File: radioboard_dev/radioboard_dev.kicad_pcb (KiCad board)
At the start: 2 copper layers, 92 parts, among them J1 Conn_01x02, J2 Conn_01x02, J3 Conn_01x04, J4 Conn_01x04, J5 Conn_01x04, J6 Conn_01x04, U10 STM32WL55CCUx, U2 TPS73733QDRBRQ1, U5 MCP73831T-2ACI_OT, U7 MAX17048G_T10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

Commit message: footprints
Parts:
- removed R36: ~, parts:R0402
- added U1: ACS722LLCTR-05AB-T, parts:SOIC127P600X175-8N, F.Cu at (86.2, 83.2)
- moved CN12 49.9 mm to (53.3, 26.1), turned to 180 degrees
- moved C10 42.1 mm to (99.1, 55.4), turned to 180 degrees
- moved C18 32.6 mm to (103.8, 47.9), turned to 90 degrees
- moved U10 29.9 mm to (104.5, 53.1)
- moved C28 29.4 mm to (105.2, 47.9), turned to -90 degrees
- moved C23 28.8 mm to (107.2, 47.9), turned to 90 degrees
- moved C26 18.1 mm to (105.3, 45.6), turned to -90 degrees
- moved J4 17.7 mm to (25.3, 38.9)
- moved J3 17.0 mm to (25.8, 64.5)
- moved LED4 16.6 mm to (87.0, 58.3), turned to 90 degrees
- moved J6 8.59 mm to (25.9, 24.4)
- moved R26 5.48 mm to (96.7, 73.8)
- moved LED2 5.20 mm to (91.0, 58.4), turned to 90 degrees
- moved LED3 4.99 mm to (92.4, 58.5), turned to 90 degrees
- moved J5 4.89 mm to (24.4, 52.8)
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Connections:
- net /U_STM32_microcontroller_IOs/BUT1 renamed BUT1
- C10 pad 1: Net-(U10-VBAT) -> +3.3V
- C18 pad 1: Net-(U10-VBAT) -> +3.3V
- C23 pad 1: Net-(U10-VBAT) -> +3.3V
- J5 pad 1: unconnected-(J5-Pin_1-Pad1) -> SPI1_MOSI
- J5 pad 2: unconnected-(J5-Pin_2-Pad2) -> SPI1_MISO
- J5 pad 4: unconnected-(J5-Pin_4-Pad4) -> SPI1_NSS
- R34 pad 1: /U_STM32_microcontroller_IOs/LED3 -> LED2
- R35 pad 1: /U_STM32_microcontroller_IOs/LED2 -> LED1
- U10 pad 11: Net-(U10-VBAT) -> +3.3V
- U10 pad 12: /U_STM32_microcontroller_IOs/LED1 -> LED1
- U10 pad 13: /U_STM32_microcontroller_IOs/LED2 -> LED2
- U10 pad 14: /U_STM32_microcontroller_IOs/LED3 -> unconnected-(U10-PA6-Pad14)
- U10 pad 37: Net-(U10-VBAT) -> +3.3V
- U10 pad 44: Net-(U10-VBAT) -> +3.3V
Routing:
- net +3.3V: track 0.00 -> 4.14 mm
- net Net-(U10-VDDA): track 0.00 -> 3.96 mm

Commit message: all footprints done
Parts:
- removed U7: MAX17048G_T10, parts:SON50P200X200X80-9N
- removed U9: TPS22917DBVR, parts:SOT95P280X145-6N
- added J9: Conn_01x04, Connector_PinHeader_2.54mm:PinHeader_1x04_P2.54mm_Vertical, F.Cu at (23.7, 69.0)
- added L1: ~, Inductor_SMD:L_0603_1608Metric, F.Cu at (92.6, 43.3)
- added L12: ~, Inductor_SMD:L_0402_1005Metric, F.Cu at (92.1, 39.1)
- added L13: ~, Inductor_SMD:L_0805_2012Metric, F.Cu at (94.5, 35.5)
- added U11: MAX17048G_T10, parts:SON50P200X200X80-9N, F.Cu at (74.0, 76.2)
- added U12: TPS73733QDRBRQ1, parts:IC_DRV8601DRBT, F.Cu at (49.2, 51.7)
- added U13: ACS722LLCTR-05AB-T, parts:SOIC127P600X175-8N, F.Cu at (44.3, 61.7)
- added XTAL1: NX2016SA-32M-EXS00A-CS06465, parts:NX2016SA_NDK, F.Cu at (121.5, 43.4)
- added XTAL2: NX2012SA-32.768K-STD-MUB-1, parts:XTAL_NX2012SA_NDK, F.Cu at (112.5, 69.2)
- added Y1: ECS-TXO-25CSMV-320-DY-TR, parts:OSC_ECS-TXO-25CSMV-320-DY-TR, F.Cu at (103.4, 29.9)
- U1: value ACS722LLCTR-05AB-T -> TPS22917DBVR; footprint parts:SOIC127P600X175-8N -> parts:SOT95P280X145-6N
- U2: value TPS73733QDRBRQ1 -> SAM-M10Q-00B; footprint parts:IC_DRV8601DRBT -> parts:SAM-M10Q_UBL
- moved U2 19.7 mm to (75.7, 95.0)
- moved J3 17.6 mm to (23.7, 82.0)
- moved J4 5.32 mm to (23.8, 44.0)
- moved J6 5.31 mm to (24.2, 29.4)
- moved J5 3.31 mm to (23.8, 56.1)
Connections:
- net /U_STM32_microcontroller_IOs/OSC32_IN renamed /microcontroller_IOs/OSC32_IN
- net /U_STM32_microcontroller_IOs/OSC32_OUT renamed /microcontroller_IOs/OSC32_OUT
- net /U_STM32_microcontroller_RF/FE_CTRL1 renamed /microcontroller_RF/FE_CTRL1
- net /U_STM32_microcontroller_RF/FE_CTRL2 renamed /microcontroller_RF/FE_CTRL2
- net /U_STM32_microcontroller_RF/FE_CTRL3 renamed /microcontroller_RF/FE_CTRL3
- C1 pad 2: Net-(U1-IP+) -> Net-(U12-OUT)
- J3 pad 1: +3.3V -> VGPS
- J3 pad 2: SCL -> GPSTXD
- J3 pad 3: SDA -> GPSRXD
- U1 pad 1: Net-(U1-IP+) -> +3.3V
- U1 pad 2: Net-(U1-IP+) -> GND
- U1 pad 3: +3.3V -> GPSPOW
- U1 pad 4: +3.3V -> unconnected-(U1-CT-Pad4)
- U1 pad 5: GND -> unconnected-(U1-QOD-Pad5)
- U1 pad 6: GND -> VGPS
- U2 pad 1: Net-(U1-IP+) -> GND
- U2 pad 10: (no net) -> GND
- U2 pad 11: (no net) -> GND
- U2 pad 12: (no net) -> SCL
- U2 pad 13: (no net) -> GPSTXD
- U2 pad 2: (no net) -> VGPS
- U2 pad 5: VBAT -> GND
- U2 pad 6: (no net) -> GND
- U2 pad 7: (no net) -> unconnected-(U2-TIMEPULSE-Pad7)
- U2 pad 8: VBAT -> unconnected-(U2-SAFEBOOT_N-Pad8)
- U2 pad 9: GND -> SDA

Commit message: pcb snapshot
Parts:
- moved C18 48.2 mm to (55.6, 45.6)
- moved C23 48.2 mm to (59.1, 45.6)
- moved C26 48.2 mm to (57.1, 43.4)
- moved C28 48.2 mm to (57.1, 45.6)
- moved U10 48.2 mm to (56.4, 50.9)
- moved C10 48.2 mm to (51.0, 53.1)
- moved U4 40.5 mm to (41.2, 47.6), turned to 180 degrees
- moved U8 38.0 mm to (41.3, 40.2), turned to 90 degrees
- moved C22 33.4 mm to (38.4, 45.5)
- moved C24 31.3 mm to (40.4, 46.5)
- moved C11 30.8 mm to (33.8, 40.9)
- moved C7 30.8 mm to (33.8, 37.5)
- moved L3 30.8 mm to (33.9, 46.3)
- moved C15 30.7 mm to (37.8, 44.0), turned to 90 degrees
- moved C12 30.6 mm to (34.0, 43.9)
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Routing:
- net Net-(C13-Pad2): track 0.00 -> 7.34 mm
- net Net-(C11-Pad2): track 0.00 -> 7.34 mm
- net GND: track 0.00 -> 5.76 mm
- net (no net): track 0.00 -> 5.07 mm
- net Net-(U8-RFin): track 0.00 -> 4.79 mm
- net Net-(U8-RF3): track 0.00 -> 4.26 mm
- net Net-(C15-Pad1): track 0.00 -> 4.15 mm
- net Net-(CN12-RF): track 0.00 -> 3.50 mm
- net Net-(U4-Y0): track 0.00 -> 2.53 mm
- net Net-(U4-Y1): track 0.00 -> 2.53 mm
- net Net-(C2-Pad1): track 0.00 -> 1.82 mm
- net Net-(C13-Pad1): track 0.00 -> 0.93 mm

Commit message: changed parts to 400MHz version
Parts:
- removed C17, C22, C92, C93, C97: Capacitor, parts:C0402
- removed C21: ~, parts:C0402
- removed R41: ~, parts:R0402
- added C29: ~, parts:C0603, F.Cu at (113.6, 30.6)
- added C32: ~, parts:C0402, F.Cu at (113.3, 32.6)
- added R5: 0, Resistor_SMD:R_0402_1005Metric, F.Cu at (28.8, 46.7)
- added R6: 0, Resistor_SMD:R_0402_1005Metric, F.Cu at (32.4, 55.2)
- C11: value Capacitor -> 15 pF; footprint parts:C0402 -> Capacitor_SMD:C_0402_1005Metric
- C13, C8: value ~ -> Capacitor
- C14: value ~ -> 15 pF; footprint parts:C0402 -> Capacitor_SMD:C_0402_1005Metric
- C15: value Capacitor -> 4.3 pF; footprint parts:C0402 -> Capacitor_SMD:C_0402_1005Metric
- C16: value ~ -> 3.6 pF; footprint parts:C0402 -> Capacitor_SMD:C_0402_1005Metric
- C19: value ~ -> 4.7pF
- C2, C24, C25, C78, C80, C82: value ~ -> 68pF; footprint parts:C0402 -> Capacitor_SMD:C_0402_1005Metric
- C5, C6: value ~ -> 6.8pF
- L10, L9: value ~ -> 0R; footprint parts:IND_0402_MURATA_LQW15AN_H0P5 -> Inductor_SMD:L_0402_1005Metric
- L11: value Inductor -> 33nH
- L2: value ~ -> 16nH; footprint parts:IND_0402_MURATA_LQW15AN_H0P5 -> Inductor_SMD:L_0402_1005Metric
- L3: value Inductor -> 16nH; footprint parts:IND_0402_MURATA_LQW15AN_H0P5 -> Inductor_SMD:L_0402_1005Metric
- L4: value ~ -> 18nH; footprint parts:IND_0402_MURATA_LQW15AN_H0P5 -> Inductor_SMD:L_0402_1005Metric
- L5: value Inductor -> 6.8nH; footprint parts:IND_0402_MURATA_LQW15AN_H0P5 -> Inductor_SMD:L_0402_1005Metric
- L6: value Inductor -> 8.2nH; footprint parts:IND_0402_MURATA_LQW15AN_H0P5 -> Inductor_SMD:L_0402_1005Metric
- L7: value Inductor -> 56nH; footprint parts:IND_0402_MURATA_LQW15AN_H0P5 -> Inductor_SMD:L_0402_1005Metric
- L8: value ~ -> 68nH; footprint parts:IND_0402_MURATA_LQW15AN2N4C00X -> Inductor_SMD:L_0402_1005Metric
- moved XTAL1 91.9 mm to (30.0, 52.5)
- moved R27 44.5 mm to (33.0, 43.8)
- moved R28 44.0 mm to (33.0, 42.7)
- moved R29 43.7 mm to (33.0, 41.6), turned to 180 degrees
- moved C31 42.0 mm to (29.6, 55.2)
- moved C30 40.4 mm to (29.9, 48.8)
- moved C71 37.1 mm to (35.5, 42.7), turned to 180 degrees
- moved C72 37.0 mm to (35.5, 43.8), turned to 180 degrees
- moved C73 36.4 mm to (35.5, 41.6), turned to 180 degrees
- moved C19 29.7 mm to (45.8, 45.2), turned to -90 degrees
- moved U2 29.6 mm to (104.6, 88.6)
- moved C20 27.3 mm to (46.7, 45.2)
- moved L11 26.4 mm to (46.2, 46.7), turned to 0 degrees
- moved C26 25.2 mm to (42.4, 63.8), turned to 90 degrees
- moved C23 24.5 mm to (40.5, 61.5), turned to -90 degrees
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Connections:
- C14 pad 2: Net-(C13-Pad2) -> Net-(C13-Pad1)
- C16 pad 1: Net-(C13-Pad2) -> Net-(C16-Pad1)
- C16 pad 2: Net-(C16-Pad2) -> Net-(C13-Pad1)
- C25 pad 1: GND -> Net-(U4-Y1)
- C25 pad 2: Net-(U4-Y1) -> GND
- C30 pad 2: OSC_IN -> Net-(C30-Pad2)
- C38 pad 2: OSC_OUT -> Net-(C38-Pad2)
- C80 pad 1: GND -> VDDRF1V55
- C80 pad 2: VDDRF1V55 -> GND
- L10 pad 2: Net-(C16-Pad2) -> Net-(C16-Pad1)
- L4 pad 1: Net-(C13-Pad1) -> Net-(C13-Pad2)
- L6 pad 1: Net-(C16-Pad2) -> Net-(C16-Pad1)
- L6 pad 2: Net-(C13-Pad2) -> Net-(C13-Pad1)
- L8 pad 2: Net-(C16-Pad2) -> Net-(C16-Pad1)
- XTAL1 pad 1: OSC_IN -> Net-(C30-Pad2)
- XTAL1 pad 3: OSC_OUT -> Net-(C38-Pad2)
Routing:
- net Net-(U8-V1): track 0.00 -> 12.0 mm, vias 0 -> 2
- net Net-(U8-RF1): track 0.00 -> 11.0 mm
- net Net-(U8-V2): track 0.00 -> 10.2 mm, vias 0 -> 2
- net Net-(U8-VDD): track 0.00 -> 9.11 mm, vias 0 -> 2
- net RFI_N: track 0.00 -> 7.70 mm
- net Net-(C13-Pad2): track 7.34 -> 0.00 mm
- net RFI_P: track 0.00 -> 7.22 mm
- net (no net): track 5.07 -> 10.4 mm
- net Net-(C16-Pad1): track 0.00 -> 4.37 mm
- net Net-(U8-RF2): track 0.00 -> 4.12 mm
- net RFO_LP: track 0.00 -> 3.59 mm
- net RFO_HP: track 0.00 -> 3.59 mm
- net GND: track 5.76 -> 3.19 mm
- net Net-(C11-Pad2): track 7.34 -> 9.70 mm
- net Net-(C12-Pad2): track 0.00 -> 0.93 mm
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
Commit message: done for day
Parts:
- C37: footprint parts:C0402 -> Capacitor_SMD:C_0402_1005Metric
- moved C29 87.7 mm to (52.0, 93.1)
- moved C32 87.7 mm to (51.7, 95.0)
- moved U13 85.6 mm to (113.0, 28.9)
- moved J4 73.1 mm to (96.8, 40.4)
- moved J5 73.1 mm to (96.8, 52.5)
- moved J6 73.1 mm to (97.3, 25.9)
- moved J9 73.1 mm to (96.7, 65.5)
- moved Y1 61.1 mm to (28.7, 58.5), turned to 90 degrees
- moved U1 59.3 mm to (31.0, 104.8)
- moved U2 59.3 mm to (49.4, 110.2)
- moved L1 54.8 mm to (40.9, 61.5), turned to 90 degrees
- moved L12 54.6 mm to (31.2, 59.7)
- moved R2 53.5 mm to (28.4, 56.3)
- moved C9 53.1 mm to (111.7, 47.3)
- moved J1 53.1 mm to (103.7, 52.0)
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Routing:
- net /microcontroller_RF/FE_CTRL2: track 0.00 -> 25.8 mm, vias 0 -> 2
- net /microcontroller_RF/FE_CTRL3: track 0.00 -> 25.4 mm, vias 0 -> 2
- net /microcontroller_RF/FE_CTRL1: track 0.74 -> 24.4 mm, vias 0 -> 3
- net VR_PA: track 0.52 -> 6.06 mm, vias 0 -> 2
- net Net-(Y1-VDD): track 0.00 -> 4.40 mm
- net VDDRF: track 0.00 -> 2.26 mm
- net VDDRF1V55: track 0.00 -> 1.82 mm
- net (no net): track 10.4 -> 8.71 mm
- net BOOT0: track 0.00 -> 1.69 mm
- net Net-(U10-VDDA): track 3.96 -> 5.46 mm
- net Net-(Y1-OUTPUT): track 0.00 -> 1.30 mm
- net Net-(C31-Pad1): track 0.00 -> 1.10 mm
- net VDD_APP: track 0.83 -> 1.55 mm, vias 0 -> 2

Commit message: roughly placed
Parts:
- added BT1: BH-18650-PC, parts:BAT_BH-18650-PC, F.Cu at (43.0, 128.2)
- C18: footprint parts:C0402 -> Capacitor_SMD:C_0402_1005Metric
- moved LED4 149.9 mm to (25.2, 156.7), turned to -90 degrees
- moved C4 145.3 mm to (26.5, 159.0)
- moved C3 145.1 mm to (30.3, 159.0), turned to 180 degrees
- moved R1 140.2 mm to (29.8, 154.2), turned to 180 degrees
- moved R3 137.2 mm to (27.2, 154.2), turned to 180 degrees
- moved U11 136.9 mm to (24.5, 152.0), turned to 180 degrees
- moved C9 134.8 mm to (26.8, 151.9), turned to 90 degrees
- moved J1 133.5 mm to (29.5, 163.0)
- moved U5 128.4 mm to (28.5, 156.8)
- moved J4 116.9 mm to (29.5, 136.0)
- moved J2 116.4 mm to (29.5, 151.0), turned to 180 degrees
- moved U13 96.8 mm to (29.2, 77.5), turned to 180 degrees
- moved J5 95.9 mm to (29.5, 120.9)
- moved U12 94.9 mm to (29.2, 84.0), turned to -90 degrees
- moved J6 93.8 mm to (29.5, 90.8)
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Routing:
- net VBAT: track 0.00 -> 90.1 mm, vias 0 -> 2
- net BOOT0: track 1.69 -> 21.1 mm, vias 0 -> 2
- net /microcontroller_IOs/OSC32_IN: track 0.00 -> 8.36 mm
- net /microcontroller_IOs/OSC32_OUT: track 0.00 -> 6.92 mm
- net VDDRF: track 2.26 -> 9.13 mm
- net Net-(U10-VDDA): track 5.46 -> 10.5 mm
- net NRST: track 0.00 -> 4.35 mm
- net BUT1: track 0.00 -> 4.35 mm
- net VLXSMPS: track 0.00 -> 4.31 mm
- net VDDRF1V55: track 1.82 -> 5.79 mm
- net Net-(U5-PROG): track 0.00 -> 3.45 mm
- net Net-(U5-STAT): track 0.00 -> 2.32 mm
- net Net-(LED4-Pad1): track 0.00 -> 2.25 mm
- net Net-(LED3-Pad1): track 0.00 -> 1.50 mm
- net Net-(LED2-Pad1): track 0.00 -> 1.50 mm
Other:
- board text added: "+5"
- board text added: "3V3"
- board text added: "CHG"
- board text added: "CLK"
- board text added: "DEBUG"
- board text added: "DIO"
- board text added: "GND"
- board text added: "I2C"
- board text added: "MISO"
- board text added: "MOSI"
- board text added: "RX"
- board text added: "SCK"
- board text added: "SCL"
- board text added: "SDA"
- board text added: "SERIAL"
- board text added: "SPI"
- board text added: "SS"
- board text added: "TX"

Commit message: almost done!!!
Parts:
- moved B4 29.0 mm to (51.2, 48.5)
- moved C67 27.8 mm to (52.5, 46.0)
- moved R26 11.4 mm to (53.2, 40.9)
- moved R4 11.4 mm to (53.2, 43.7)
- moved B1 9.58 mm to (25.2, 37.0), turned to 90 degrees
- moved LED3 9.50 mm to (24.8, 31.5), turned to 180 degrees
- moved C31 9.44 mm to (34.0, 50.4), turned to 180 degrees
- moved LED2 9.03 mm to (24.8, 33.2), turned to 180 degrees
- moved R2 7.90 mm to (34.0, 51.5), turned to 0 degrees
- moved C30 7.32 mm to (31.0, 51.2), turned to -90 degrees
- moved R6 7.01 mm to (31.0, 55.7), turned to 90 degrees
- moved R34 6.00 mm to (27.4, 31.5), turned to 180 degrees
- moved R5 5.58 mm to (29.5, 51.2), turned to 90 degrees
- moved XTAL1 5.34 mm to (30.3, 53.4), turned to 0 degrees
- moved C38 5.31 mm to (29.5, 55.7), turned to 90 degrees
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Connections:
- U10 pad 14: unconnected-(U10-PA6-Pad14) -> BUT1
- U10 pad 15: BUT1 -> unconnected-(U10-PA7-Pad15)
- U10 pad 16: GPSPOW -> unconnected-(U10-PA8-Pad16)
- U10 pad 17: SCL -> unconnected-(U10-PA9-Pad17)
- U10 pad 33: SDA -> unconnected-(U10-PA10-Pad33)
- U10 pad 4: /microcontroller_RF/FE_CTRL1 -> SCL
- U10 pad 43: unconnected-(U10-PA15-Pad43) -> GPSPOW
- U10 pad 5: /microcontroller_RF/FE_CTRL2 -> SDA
- U10 pad 6: /microcontroller_RF/FE_CTRL3 -> /microcontroller_RF/FE_CTRL1
- U10 pad 7: unconnected-(U10-PA0-Pad7) -> /microcontroller_RF/FE_CTRL2
- U10 pad 8: unconnected-(U10-PA1-Pad8) -> /microcontroller_RF/FE_CTRL3
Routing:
- net LPUART1_RX: track 0.00 -> 117.6 mm, vias 0 -> 2
- net LPUART1_TX: track 0.00 -> 114.2 mm, vias 0 -> 2
- net SPI1_SCK: track 0.00 -> 96.5 mm, vias 0 -> 2
- net SPI1_MISO: track 0.00 -> 93.7 mm, vias 0 -> 2
- net SPI1_MOSI: track 0.00 -> 90.9 mm, vias 0 -> 2
- net SPI1_NSS: track 0.00 -> 89.6 mm, vias 0 -> 2
- net SCL: track 0.00 -> 79.7 mm, vias 0 -> 6
- net SDA: track 0.00 -> 74.1 mm, vias 0 -> 4
- net SWCLK: track 0.00 -> 52.9 mm, vias 0 -> 1
- net SWDIO: track 0.00 -> 46.3 mm, vias 0 -> 1
- net VCURR: track 0.00 -> 35.0 mm, vias 0 -> 2
- net VGPS: track 0.00 -> 33.7 mm
- net CURROUT: track 0.00 -> 32.4 mm, vias 0 -> 2
- net VDDRF1V55: track 5.79 -> 26.4 mm, vias 0 -> 3
- net VDDRF: track 9.13 -> 29.6 mm, vias 0 -> 3
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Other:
- board outline added: 32.5 x 148.5 mm

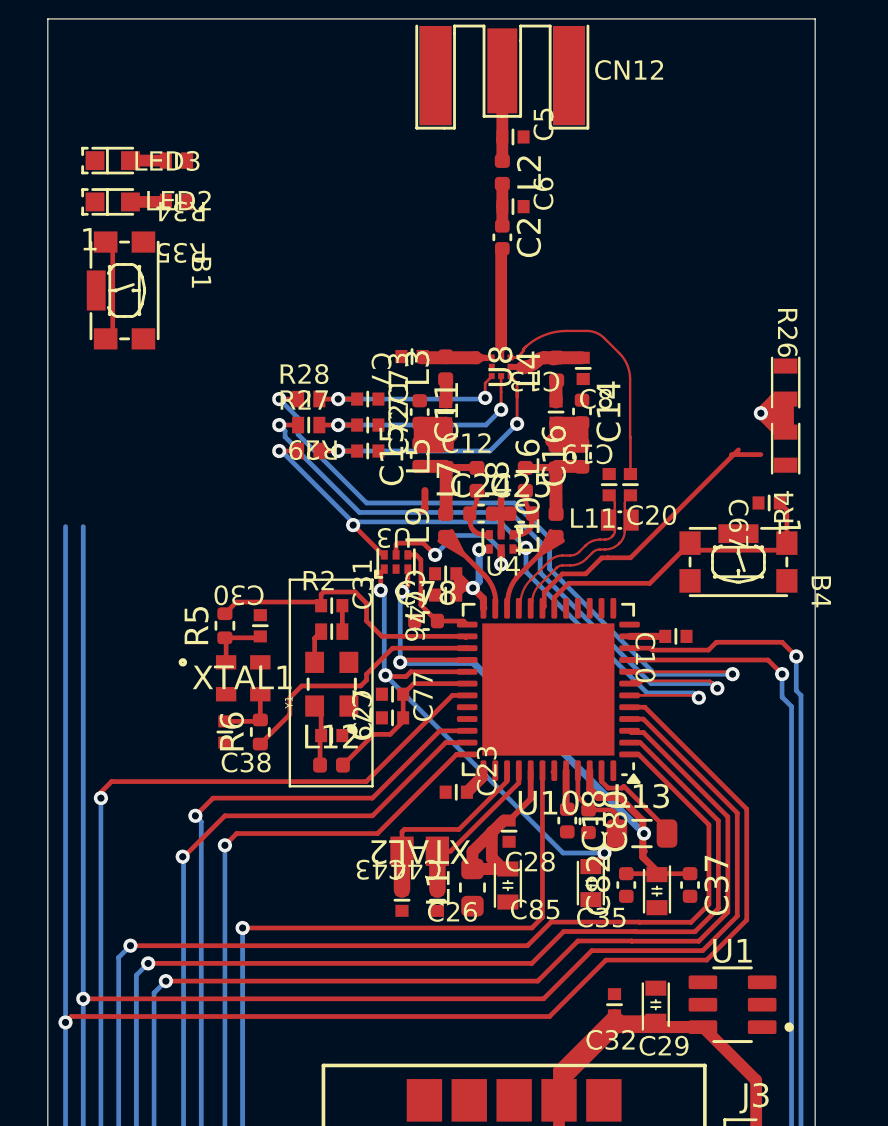
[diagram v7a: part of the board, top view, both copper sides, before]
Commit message: routing minus ground planes complete
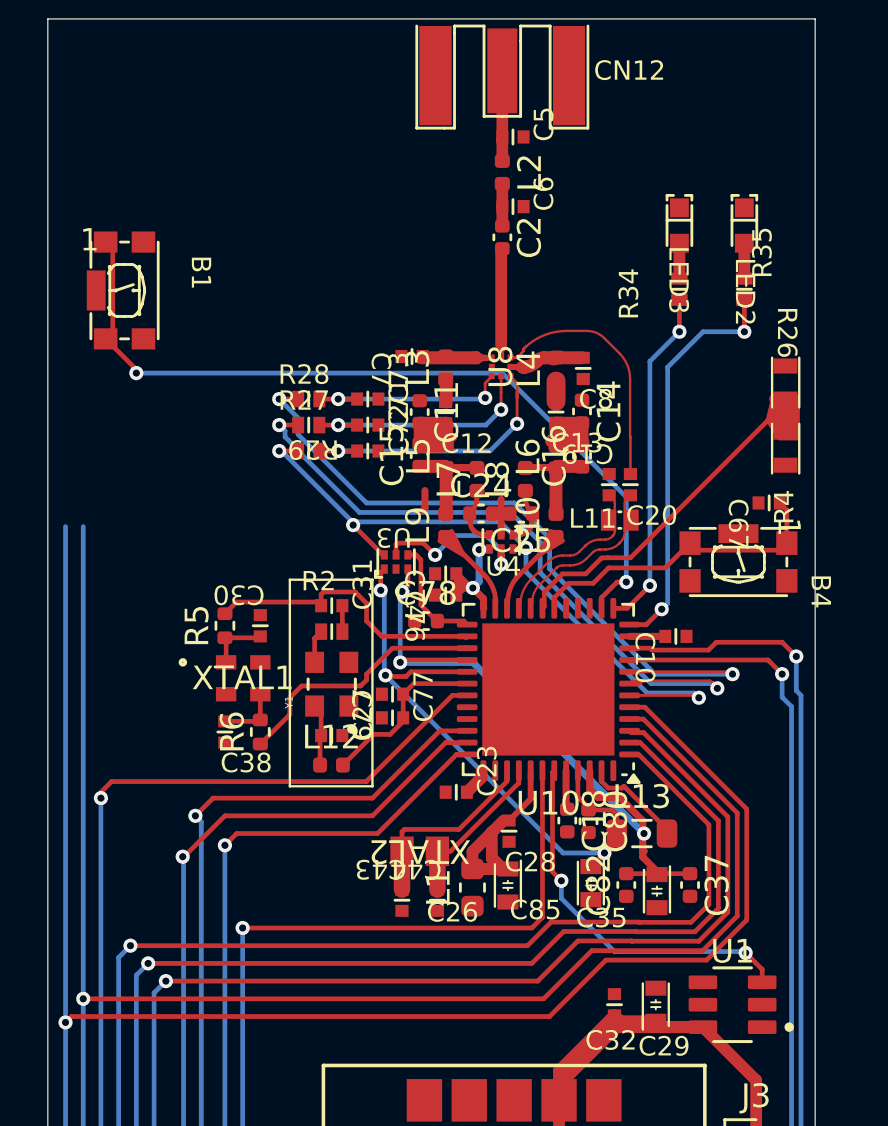
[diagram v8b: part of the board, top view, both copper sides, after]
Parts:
- moved LED2 26.8 mm to (51.5, 34.2), turned to 90 degrees
- moved R35 24.3 mm to (51.5, 37.0), turned to 90 degrees
- moved LED3 24.2 mm to (48.8, 34.2), turned to 90 degrees
- moved R34 22.0 mm to (48.8, 37.0), turned to 90 degrees
- turned C13 to 90 degrees
- turned C25 to 180 degrees
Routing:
- net BUT1: track 4.35 -> 34.6 mm, vias 0 -> 2
- net LED1: track 0.00 -> 17.2 mm, vias 0 -> 2
- net GPSPOW: track 0.08 -> 15.9 mm, vias 0 -> 2
- net LED2: track 0.00 -> 14.6 mm, vias 0 -> 2
- net (no net): track 8.71 -> 0.00 mm
- net Net-(C13-Pad1): track 0.93 -> 8.71 mm
- net Net-(C13-Pad2): track 0.00 -> 0.90 mm
- net BOOT0: track 17.7 -> 17.4 mm, vias 1 -> 0
